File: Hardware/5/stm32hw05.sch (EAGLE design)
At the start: 54 parts, among them CN1 AC 9V, U1 STM32F303_334RXT

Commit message: v5 design
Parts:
- removed 3V3, BATTERY: SOLDERJUMPERNO, SparkFun:SOLDERJUMPERNO
- removed C1, C2: 4.3p, resistor:C-EUC0603
- removed C7: 100nF, resistor:C-EUC0603
- removed CN1: AC 9V, adafruit:DCBARRELPTH
- removed CR1220: CR1220SMD, IotaWatt_parts:CR1220SMD
- removed LSE: 32.768kHz, crystal:MC-306
- removed T1, T2, T3, T4: (no value), con-weidmueller-sl35:180-3
- removed U1: STM32F303_334RXT, stm32f303:STM32F303_334RXT
- added DS18B20, PULSE: (no value), con-weidmueller-sl35:180-3
- added STM32: STM32F302_303C2, stm32f303cb:STM32F302_303C2
- added U$1: 2.1MMJACKSMT, adafruit:2.1MMJACKSMT
- renumbered C11 to CF1, C12 to CF2, C13 to CF3, C17 to CFV, R10 to RF2, R11 to RB3, R12 to RF3, R21 to RFV, R7 to RB1, R8 to RF1, R9 to RB2
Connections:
- removed net N$1: BATTERY.2, CR1220.P$+
- removed net N$6: U1.PB2
- removed net N$7: T1.2
- removed net N$9: T1.3
- removed net UART2_RX: GND.4, RASPBERRYPI.7
- removed net UART2_TX: GND.5, RASPBERRYPI.9
- removed net UART3_RX: U1.PB11
- removed net UART3_TX: U1.PB10
- new net UART_RX: GND.4, RASPBERRYPI.7, STM32.PB4
- new net UART_TX: GND.5, RASPBERRYPI.9, STM32.PB3
- net +3V3: now also DS18B20.3, PULSE.3, STM32.VDD, STM32.VDDA/VREF+, STM32.VDD_2, STM32.VDD_3; no longer 3V3.1, C7.2, T1.1, U1.VDD, U1.VDDA/VREF+, U1.VDD_2, U1.VDD_3, U1.VDD_4
- net AC: now also U$1.TIP; no longer CN1.PWR
- net BIAS: now also STM32.PA6, U$1.RING, U$1.RING_SW; no longer CN1.GND, CN1.GNDBREAK, U1.PA6
- net BIAS_IN: now also STM32.PA7; no longer U1.PA7
- net BOOT0: now also STM32.BOOT0; no longer U1.BOOT0
- net CT1: now also STM32.PA0; no longer U1.PA0
- net CT2: now also STM32.PA1; no longer U1.PA1
- net CT3: now also STM32.PA2; no longer U1.PA2
- net DS18B20: now also DS18B20.2, STM32.PA9; no longer T2.1, U1.PA9
- net GND: now also DS18B20.1, PULSE.1, STM32.VSS, STM32.VSSA/VREF-, STM32.VSS_2, STM32.VSS_3; no longer C1.2, C2.2, C7.1, CR1220.P$-, T2.3, U1.VSS, U1.VSSA/VREF-, U1.VSS_2, U1.VSS_3, U1.VSS_4
- net HSE_IN: now also STM32.PF0-OSC_IN; no longer U1.PF0-OSC_IN
- net HSE_OUT: now also STM32.PF1-OSC_OUT; no longer U1.PF1-OSC_OUT
- net LED: now also STM32.PA8; no longer U1.PA8
- net LSE_IN: now also STM32.PC14-OSC32_IN; no longer C1.1, LSE.1, U1.PC14-OSC32_IN
- net LSE_OUT: now also STM32.PC15-OSC_OUT; no longer C2.1, LSE.2, U1.PC15-OSC_OUT
- net NRST: now also STM32.NRST; no longer U1.NRST
- net PULSE: now also PULSE.2, STM32.PA10; no longer T2.2, U1.PA10
- net SWCLK: now also STM32.PA14; no longer U1.PA14
- net SWDIO: now also STM32.PA13; no longer U1.PA13
- net VBAT: now also STM32.VBAT; no longer 3V3.2, BATTERY.1, U1.VBAT
- net VSIG: now also STM32.PB12; no longer U1.PB12
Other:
- note removed: "3"
- note removed: "Battery Options?"
- note removed: "Could use 3WAY 2.54mm header here?"

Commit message: gerbers
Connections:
- net +3V3: no longer RASPBERRYPI.2
- net +5V: now also RASPBERRYPI.1, RASPBERRYPI.3
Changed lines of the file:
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@@
 <label x="40.64" y="-30.48" size="1.778" layer="95"/>
+</segment>
+<segment>
+<pinref part="RASPBERRYPI" gate="G$1" pin="3"/>
+<pinref part="RASPBERRYPI" gate="G$1" pin="1"/>
+<wire x1="129.54" y1="-27.94" x2="129.54" y2="-30.48" width="0.1524" layer="91"/>
+<wire x1="129.54" y1="-30.48" x2="129.54" y2="-35.56" width="0.1524" layer="91"/>
+<label x="124.46" y="-35.56" size="1.778" layer="95"/>
 </segment>
 </net>
@@
 </segment>
 <segment>
-<pinref part="RASPBERRYPI" gate="G$1" pin="2"/>
-<wire x1="144.78" y1="-30.48" x2="152.4" y2="-30.48" width="0.1524" layer="91"/>
-<label x="152.4" y="-30.48" size="1.778" layer="95"/>
-<junction x="144.78" y="-30.48"/>
-</segment>
-<segment>

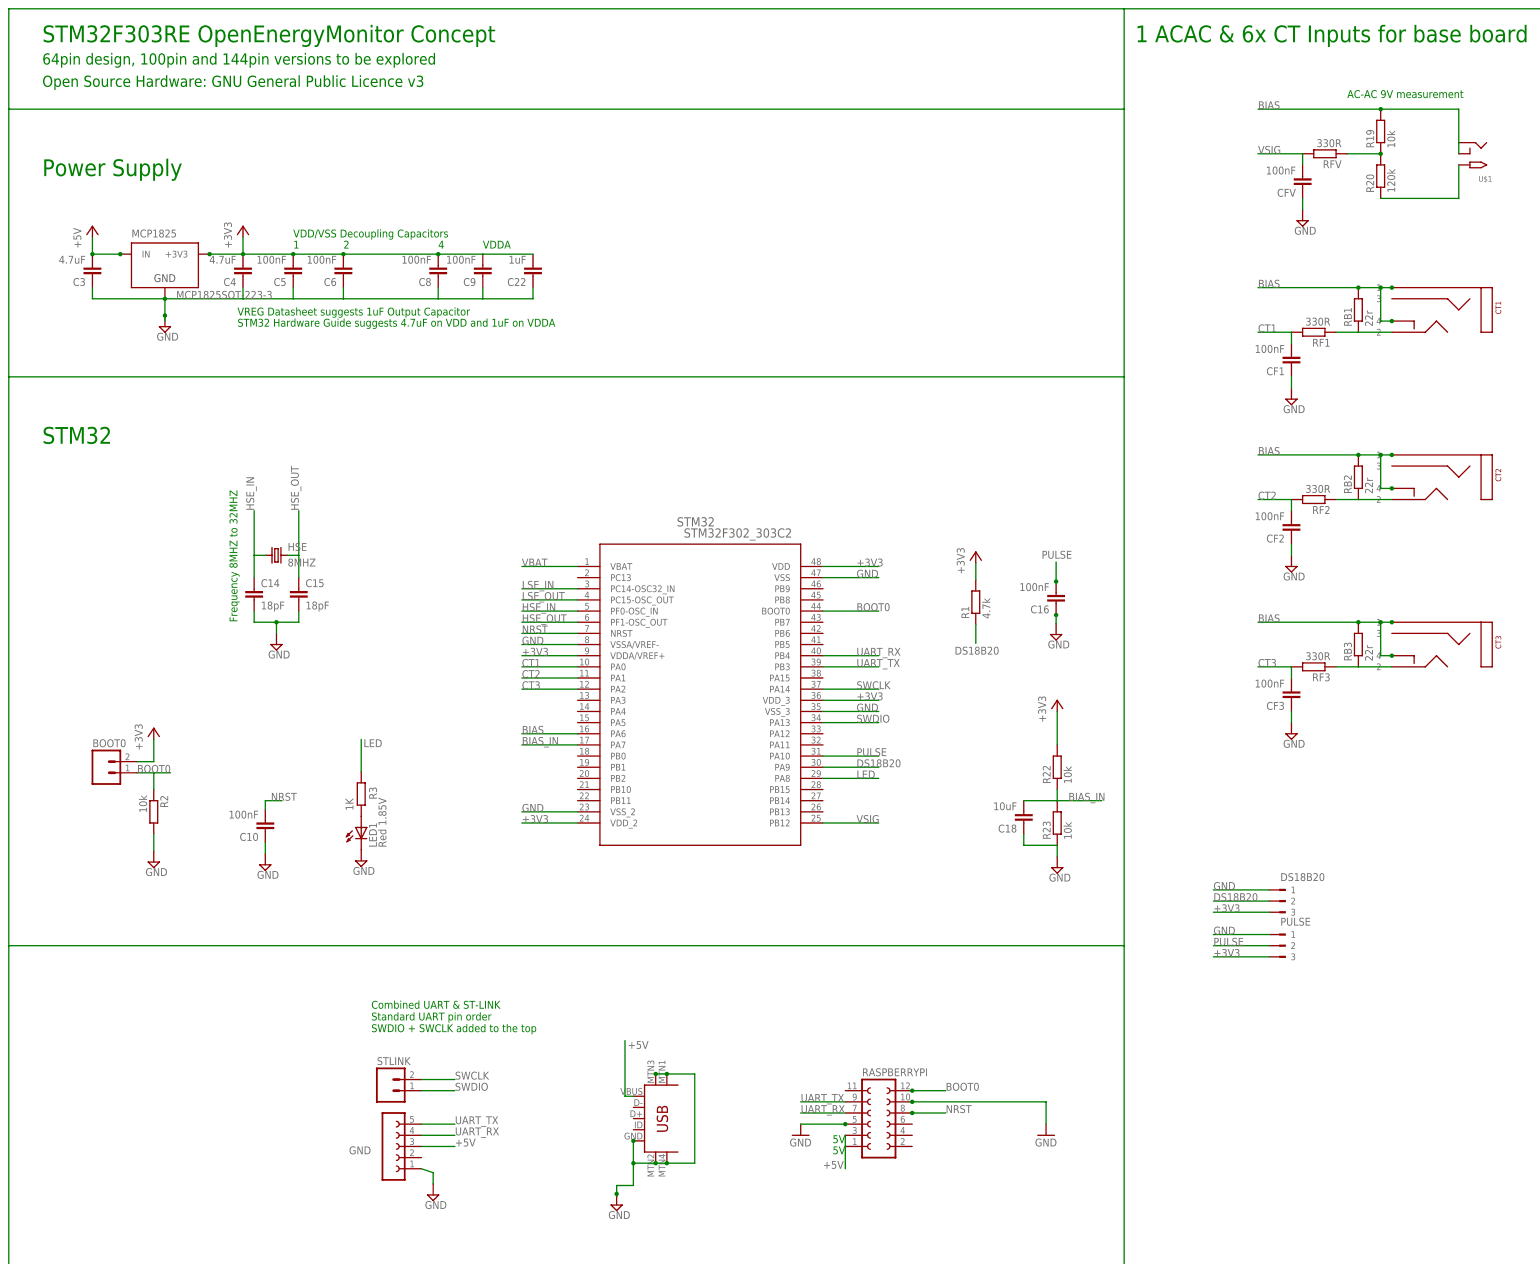
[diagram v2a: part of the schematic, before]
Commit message: added NRST & 3.3v routing
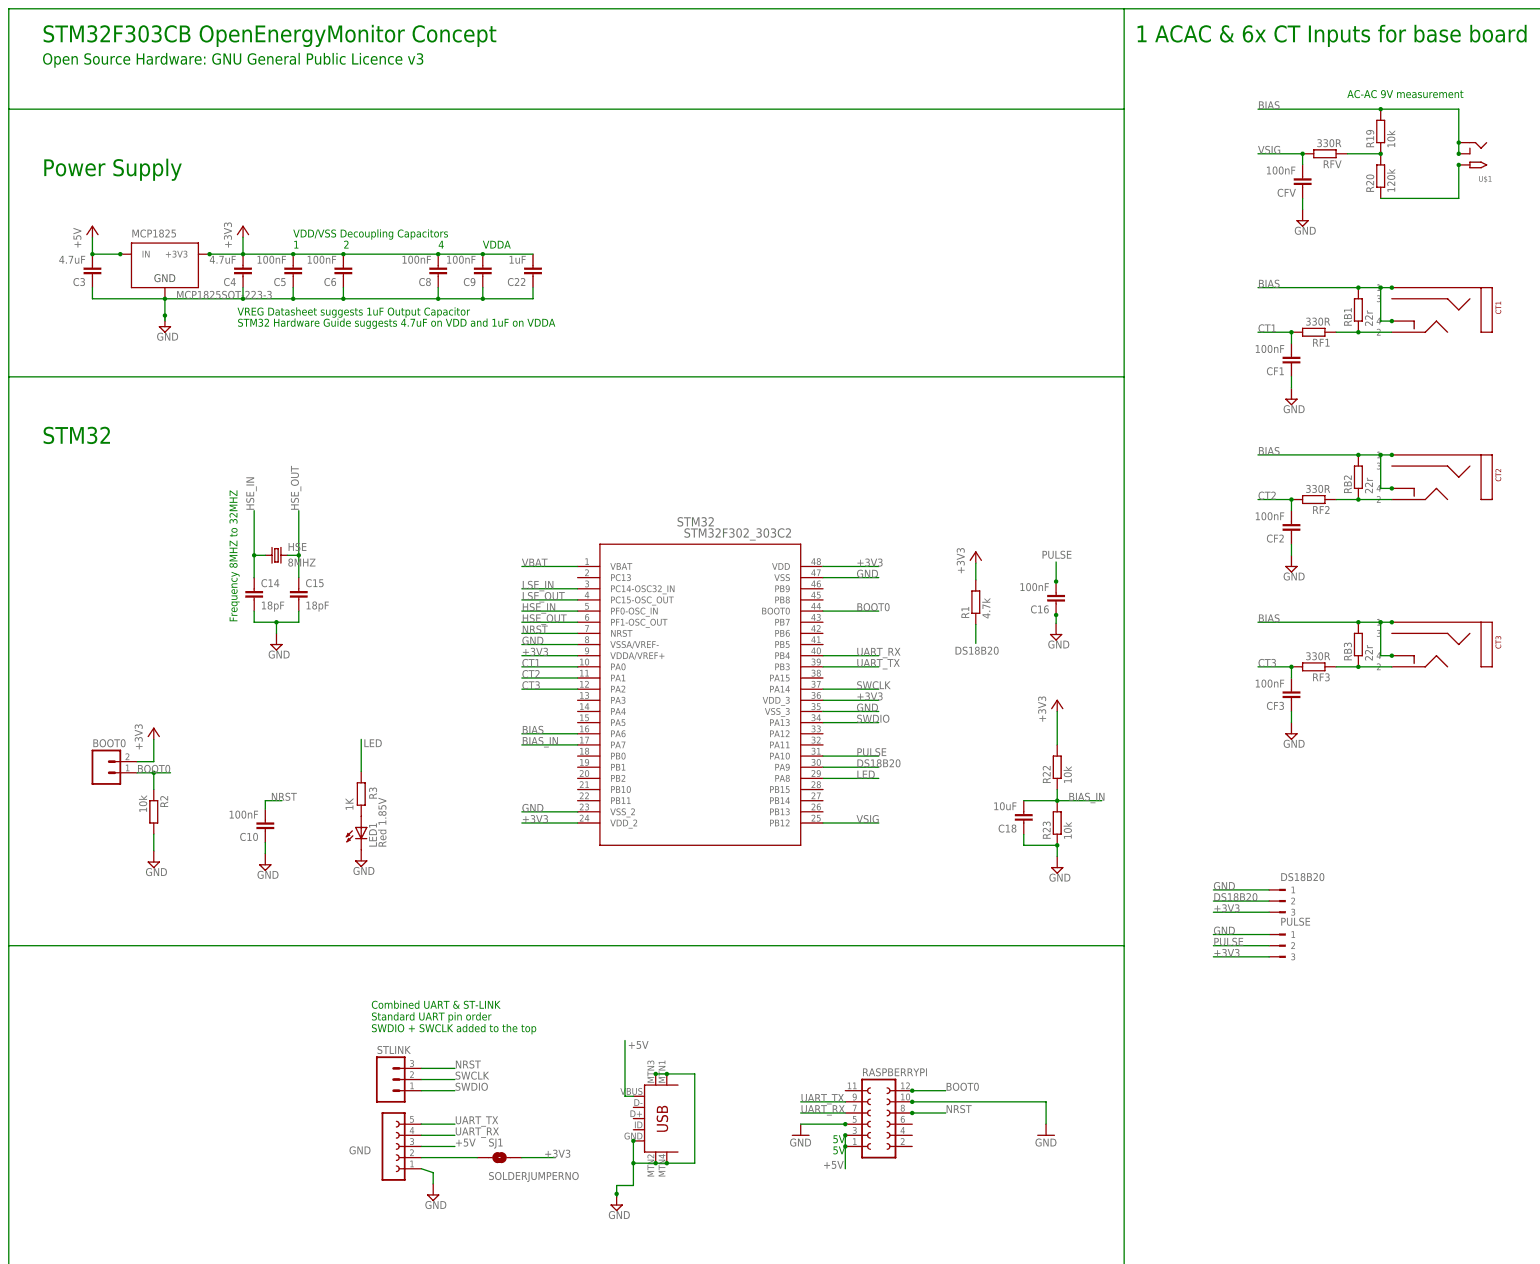
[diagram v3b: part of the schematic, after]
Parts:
- added SJ1: SOLDERJUMPERNO, SparkFun:SOLDERJUMPERNO
- STLINK: device SparkFun:M02PTH -> SparkFun:M03PTH
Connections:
- new net N$1: GND.2, SJ1.1
- net +3V3: now also SJ1.2
- net NRST: now also STLINK.3
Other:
- note added: "STM32F303CB OpenEnergyMonitor Concept"
- note removed: "64pin design, 100pin and 144pin versions to be explored"
- note removed: "STM32F303RE OpenEnergyMonitor Concept"

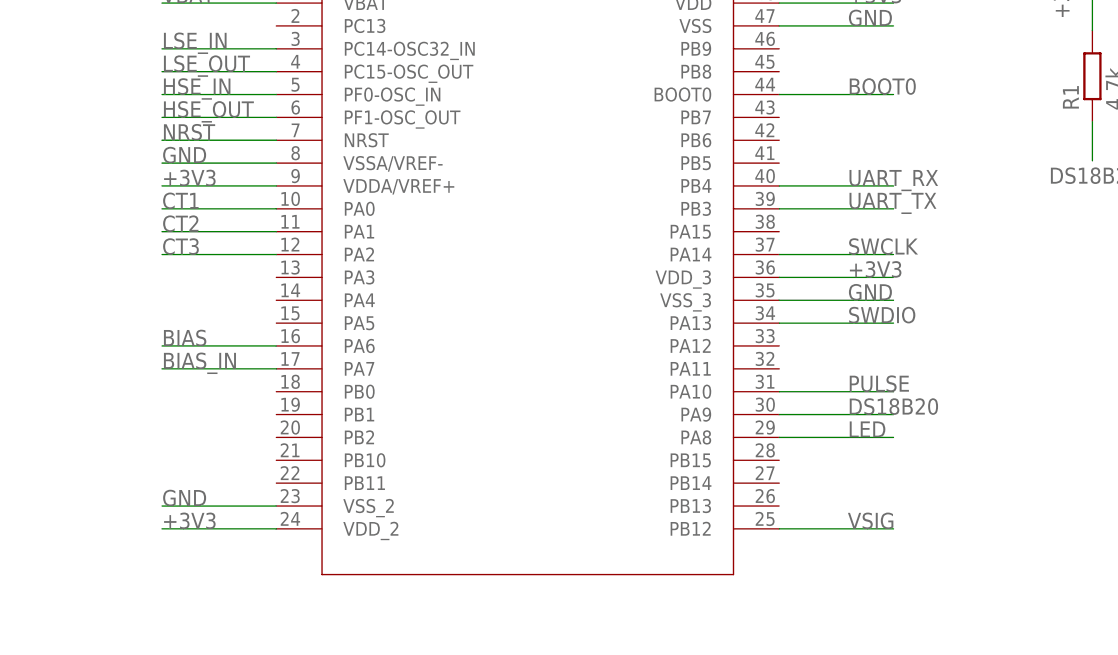
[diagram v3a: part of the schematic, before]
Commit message: move UART to PA9 & PA10, move pulse, LED & ds18b20
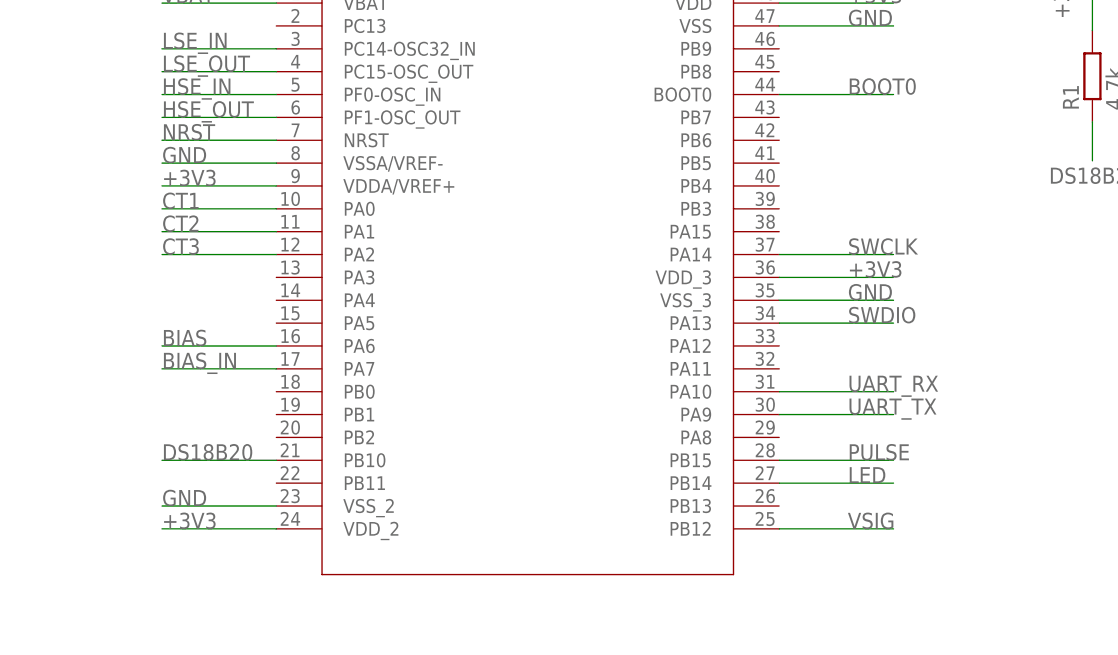
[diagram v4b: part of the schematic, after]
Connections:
- net DS18B20: now also STM32.PB10; no longer STM32.PA9
- net LED: now also STM32.PB14; no longer STM32.PA8
- net PULSE: now also STM32.PB15; no longer STM32.PA10
- net UART_RX: now also STM32.PA10; no longer STM32.PB4
- net UART_TX: now also STM32.PA9; no longer STM32.PB3
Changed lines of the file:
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@@
-</segment>
-<segment>
-<pinref part="STM32" gate="A" pin="PA9"/>
-<wire x1="124.46" y1="55.88" x2="137.16" y2="55.88" width="0.1524" layer="91"/>
-<label x="132.08" y="55.88" size="1.778" layer="95"/>
 </segment>
 <segment>
@@
 <wire x1="226.06" y1="25.4" x2="213.36" y2="25.4" width="0.1524" layer="91"/>
 <label x="213.36" y="25.4" size="1.778" layer="95"/>
+</segment>
+<segment>
+<pinref part="STM32" gate="A" pin="PB10"/>
+<wire x1="68.58" y1="50.8" x2="55.88" y2="50.8" width="0.1524" layer="91"/>
+<label x="55.88" y="50.8" size="1.778" layer="95"/>
 </segment>
 </net>
@@
 </segment>
 <segment>
-<pinref part="STM32" gate="A" pin="PA10"/>
-<wire x1="124.46" y1="58.42" x2="137.16" y2="58.42" width="0.1524" layer="91"/>
-<label x="132.08" y="58.42" size="1.778" layer="95"/>
+<pinref part="STM32" gate="A" pin="PB15"/>
+<wire x1="124.46" y1="50.8" x2="137.16" y2="50.8" width="0.1524" layer="91"/>
+<label x="132.08" y="50.8" size="1.778" layer="95"/>
 </segment>
 </net>
@@
 </segment>
 <segment>
-<pinref part="STM32" gate="A" pin="PA8"/>
-<wire x1="124.46" y1="53.34" x2="137.16" y2="53.34" width="0.1524" layer="91"/>
-<label x="132.08" y="53.34" size="1.778" layer="95"/>
+<pinref part="STM32" gate="A" pin="PB14"/>
+<wire x1="124.46" y1="48.26" x2="137.16" y2="48.26" width="0.1524" layer="91"/>
+<label x="132.08" y="48.26" size="1.778" layer="95"/>
 </segment>
 </net>
 <net name="UART_RX" class="0">
-<segment>
-<pinref part="STM32" gate="A" pin="PB4"/>
-<wire x1="124.46" y1="81.28" x2="137.16" y2="81.28" width="0.1524" layer="91"/>
-<label x="132.08" y="81.28" size="1.778" layer="95"/>
-</segment>
 <segment>
 <pinref part="GND" gate="G$1" pin="4"/>
@@
 <label x="119.38" y="-22.86" size="1.778" layer="95"/>
 </segment>
+<segment>
+<pinref part="STM32" gate="A" pin="PA10"/>
+<wire x1="124.46" y1="58.42" x2="137.16" y2="58.42" width="0.1524" layer="91"/>
+<label x="132.08" y="58.42" size="1.778" layer="95"/>
+</segment>
 </net>
 <net name="UART_TX" class="0">
-<segment>
-<pinref part="STM32" gate="A" pin="PB3"/>
-<wire x1="124.46" y1="78.74" x2="137.16" y2="78.74" width="0.1524" layer="91"/>
-<label x="132.08" y="78.74" size="1.778" layer="95"/>
-</segment>
 <segment>
 <pinref part="GND" gate="G$1" pin="5"/>
@@
 <label x="119.38" y="-20.32" size="1.778" layer="95"/>
 </segment>
+<segment>
+<pinref part="STM32" gate="A" pin="PA9"/>
+<wire x1="124.46" y1="55.88" x2="137.16" y2="55.88" width="0.1524" layer="91"/>
+<label x="132.08" y="55.88" size="1.778" layer="95"/>
+</segment>
 </net>
